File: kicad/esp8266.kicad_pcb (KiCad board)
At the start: 2 copper layers, 21 parts, among them J1 BATT, J2 Conn_Coaxial_Power, Q1 BSP75, U1 ESP-12E, U2 MCP73831-2-OT, U3 MCP1703A-3302_SOT23, U5 PCA9685PW, U6 Si7020-A20

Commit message: updates
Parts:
- added C6: 1uF, Capacitor_SMD:C_0805_2012Metric_Pad1.15x1.40mm_HandSolder, F.Cu at (280.5, 60.7)
- added C7: 1uF, Capacitor_SMD:C_0805_2012Metric_Pad1.15x1.40mm_HandSolder, F.Cu at (280.5, 62.6)
- added D3: D_Schottky, Diode_SMD:D_SOD-123, F.Cu at (249.1, 74.4)
- added D4: D_Schottky, Diode_SMD:D_SOD-123, F.Cu at (87.5, 72.5)
- added J3: CONN FT232RL, Connector_PinHeader_2.54mm:PinHeader_1x06_P2.54mm_Vertical, F.Cu at (87.5, 64.8)
- added J4: RJ12, Connector_RJ:RJ12_Amphenol_54601, F.Cu at (93.0, 127.0)
- added J5: RJ12, Connector_RJ:RJ12_Amphenol_54601, F.Cu at (93.0, 147.0)
- added J6: Onewire, Connector_Audio:Jack_3.5mm_Ledino_KB3SPRS_Horizontal, F.Cu at (168.0, 117.0)
- added J7: Onewire, Connector_Audio:Jack_3.5mm_Ledino_KB3SPRS_Horizontal, F.Cu at (193.0, 107.0)
- added Q2: BSP75, Package_TO_SOT_SMD:SOT-223-3_TabPin2, F.Cu at (118.6, 128.1)
- added Q3: BSP75, Package_TO_SOT_SMD:SOT-223-3_TabPin2, F.Cu at (127.4, 128.1)
- added Q4: BSP75, Package_TO_SOT_SMD:SOT-223-3_TabPin2, F.Cu at (118.6, 135.3)
- added R10: 10k, Resistor_SMD:R_0805_2012Metric_Pad1.15x1.40mm_HandSolder, F.Cu at (249.1, 76.5)
- added R7: 10k, Resistor_SMD:R_0805_2012Metric_Pad1.15x1.40mm_HandSolder, F.Cu at (215.2, 129.2)
- added R8: 10k, Resistor_SMD:R_0805_2012Metric_Pad1.15x1.40mm_HandSolder, F.Cu at (114.0, 72.5)
- added R9: 4.7k, Resistor_SMD:R_0805_2012Metric_Pad1.15x1.40mm_HandSolder, F.Cu at (245.3, 80.8)
- added SW1: RESET, digikey-footprints:Switch_Tactile_SMD_6x6mm, F.Cu at (149.1, 66.8)
- added SW2: PROG, digikey-footprints:Switch_Tactile_SMD_6x6mm, F.Cu at (149.1, 76.9)
- added TP1: TestPoint_2Pole, TestPoint:TestPoint_2Pads_Pitch2.54mm_Drill0.8mm, F.Cu at (258.4, 110.4)
- added U4: MS5637, libs:MS5637, F.Cu at (175.1, 58.4)
- R6: value 1M -> 270k
- U5: value PCA9685PW -> MCP1703A-5002_SOT23; footprint Package_SO:TSSOP-28_4.4x9.7mm_P0.65mm -> Package_TO_SOT_SMD:SOT-23
- moved J2 88.7 mm to (93.0, 112.0)
- moved U1 60.1 mm to (128.0, 67.0)
- moved R4 56.2 mm to (97.0, 76.2), turned to 180 degrees
- moved C1 53.9 mm to (101.3, 82.5)
- moved C2 53.9 mm to (93.8, 81.8)
- moved R1 53.9 mm to (97.5, 82.8)
- moved R3 52.4 mm to (101.6, 76.2), turned to 180 degrees
- moved R5 49.1 mm to (114.0, 64.8)
- moved C3 48.3 mm to (114.0, 69.9), turned to 180 degrees
- moved U2 46.9 mm to (107.2, 74.4), turned to 270 degrees
- moved R2 44.5 mm to (114.0, 75.0)
- moved R6 44.4 mm to (114.0, 67.4), turned to 180 degrees
- moved J1 44.1 mm to (108.5, 65.5), turned to 180 degrees
- moved D2 31.7 mm to (115.5, 81.4), turned to 180 degrees
- moved D1 31.4 mm to (115.5, 85.8)
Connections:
- net /MCP73831/STAT renamed /MCP73831/V_STATUS
- net Net-(C2-Pad1) renamed /VBAT
- net Net-(J2-Pad1) renamed +12V
- net Net-(U1-Pad16) renamed /IO15
- net Net-(U1-Pad19) renamed /SDA
- net Net-(U1-Pad20) renamed /SCL
- net Net-(U1-Pad5) renamed /IO14
- net Net-(U1-Pad6) renamed /IO12
- net Net-(U1-Pad7) renamed /IO13
- C3 pad 1: /MCP73831/VOLT -> /ADC
- C4 pad 2: VDD -> /MCP1703-33/VDD
- D1 pad 3: /MCP73831/VOUT -> /MCP1703-33/VDD
- D2 pad 1: /MCP73831/VOUT -> /MCP1703-33/VDD
- J2 pad 2: Net-(J2-Pad2) -> GND
- R5 pad 2: /MCP73831/VOLT -> /ADC
- R6 pad 1: /MCP73831/VOLT -> /ADC
- U1 pad 1: Net-(U1-Pad1) -> /RST
- U1 pad 15: Net-(U1-Pad15) -> GND
- U1 pad 17: Net-(U1-Pad17) -> /IO2
- U1 pad 2: Net-(U1-Pad2) -> /ADC
- U1 pad 21: Net-(U1-Pad21) -> /RX
- U1 pad 22: Net-(U1-Pad22) -> /TX
- U1 pad 3: Net-(U1-Pad3) -> /EN
- U1 pad 4: Net-(U1-Pad4) -> /RST
- U1 pad 8: Net-(U1-Pad8) -> +3V3
- U3 pad 3: VDD -> /MCP1703-33/VDD
- U5 pad 2: GND -> /MCP1703-50/3.3V
- U5 pad 3: GND -> /MCP1703-50/VDD
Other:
- board outline added: 100 x 100 mm

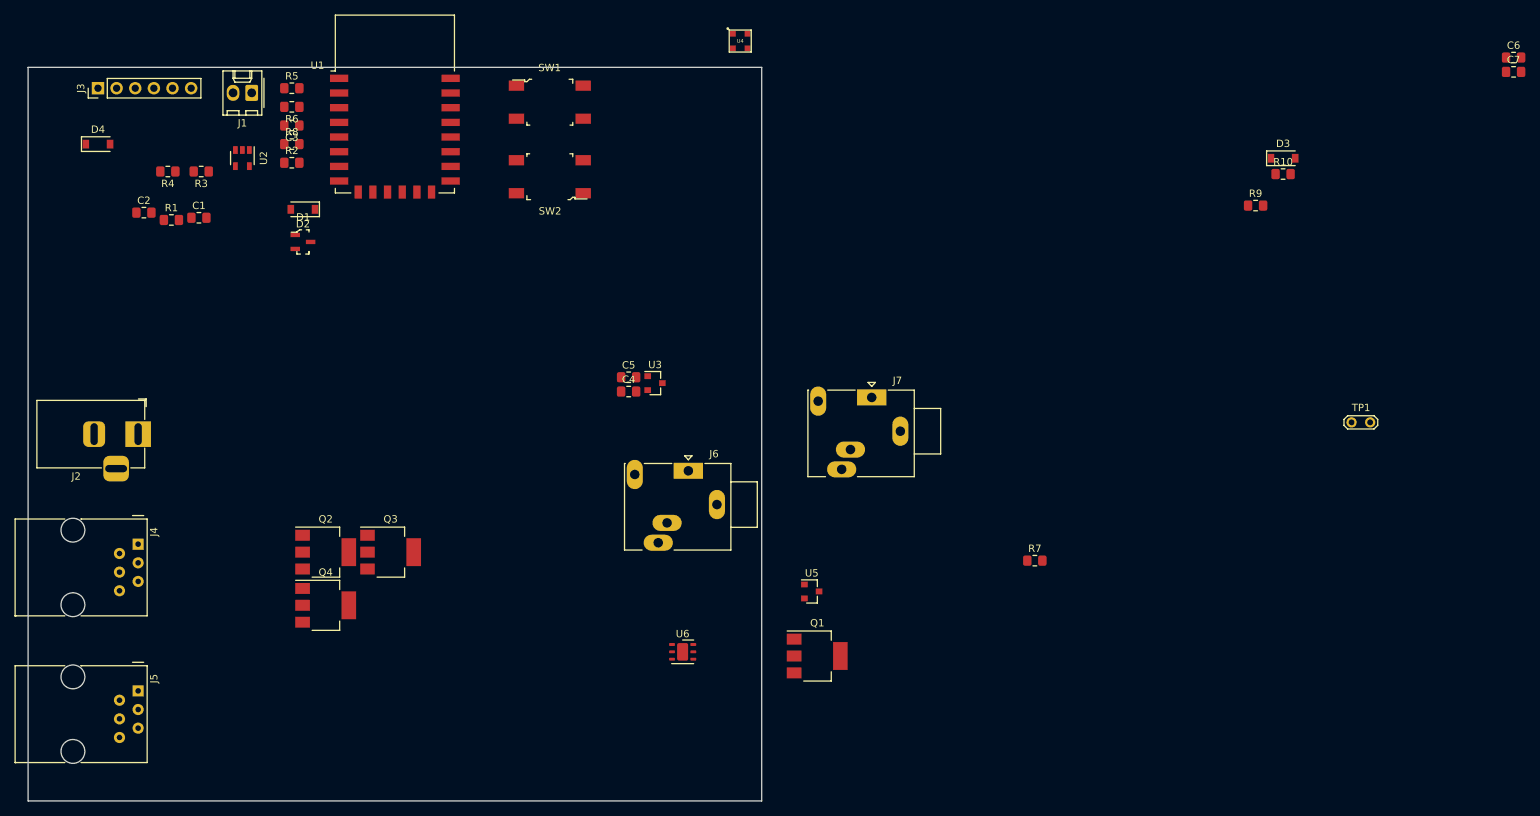
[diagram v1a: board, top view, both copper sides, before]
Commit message: add 18B20 on board
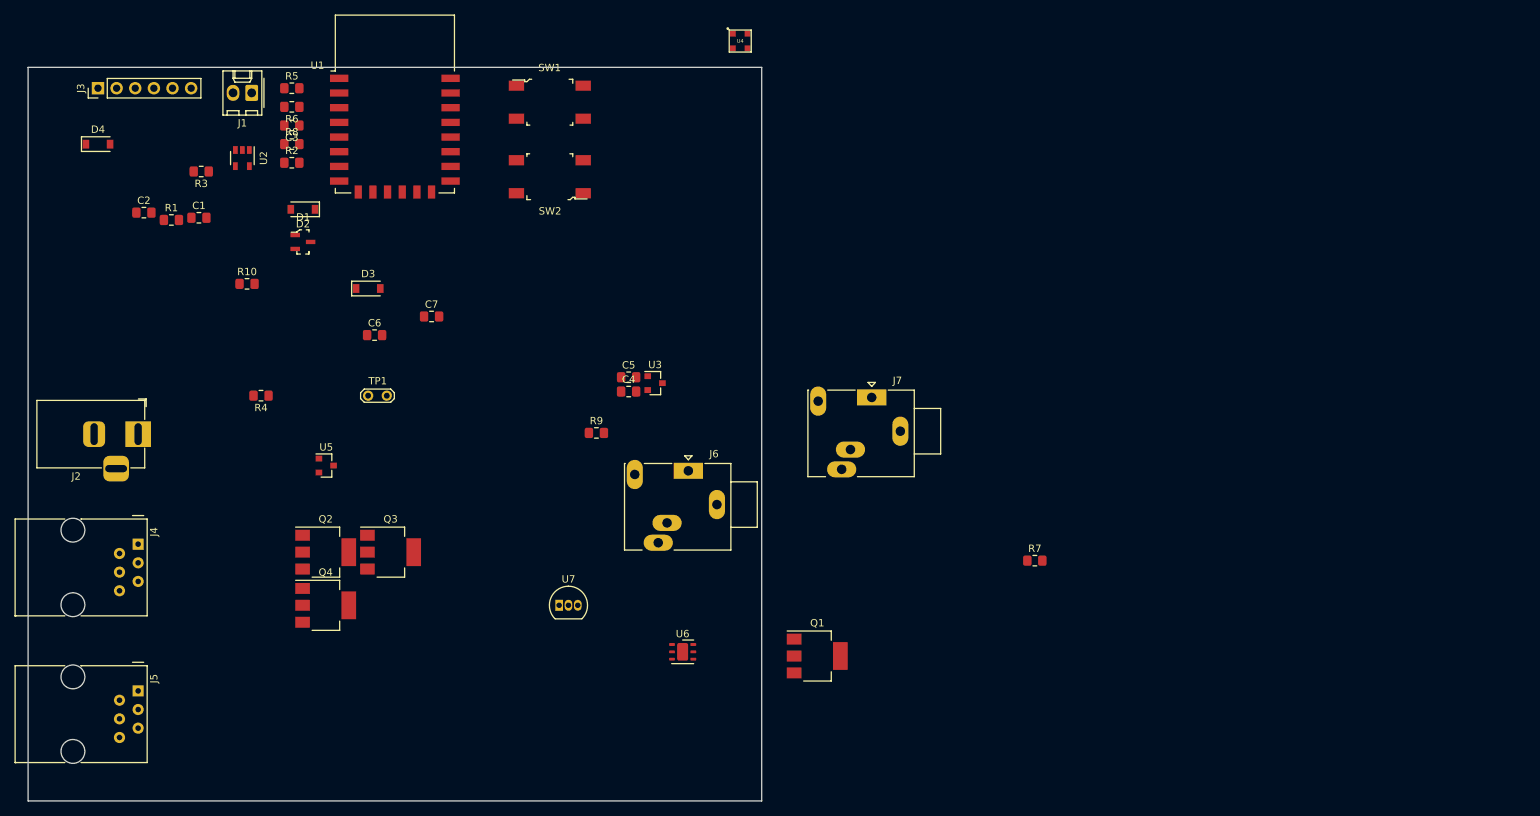
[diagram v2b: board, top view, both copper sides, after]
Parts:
- added U7: DS18B20, Package_TO_SOT_THT:TO-92_Inline, F.Cu at (150.4, 135.3)
- U2: value MCP73831-2-OT -> MCP73831-2
- moved C6 159.8 mm to (125.2, 98.5)
- moved C7 151.2 mm to (133.0, 96.0)
- moved R10 142.0 mm to (107.8, 91.5)
- moved TP1 134.1 mm to (124.4, 106.8)
- moved D3 126.0 mm to (124.4, 92.2)
- moved R9 95.0 mm to (155.5, 111.8)
- moved U5 68.4 mm to (118.6, 116.3)
- moved R4 33.1 mm to (109.8, 106.8)
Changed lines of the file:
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@@
     (tracks 0)
     (zones 0)
-    (modules 41)
-    (nets 74)
+    (modules 42)
+    (nets 77)
   )
   (page A4)
@@
   (net 72 /IO13)
   (net 73 /IO15)
+  (net 74 "Net-(U7-Pad2)")
+  (net 75 "Net-(U7-Pad3)")
+  (net 76 "Net-(U7-Pad1)")
   (net_class Default "This is the default net class."
     (clearance 0.2)
@@
     (add_net "Net-(U6-Pad6)")
     (add_net "Net-(U6-Pad7)")
+    (add_net "Net-(U7-Pad1)")
+    (add_net "Net-(U7-Pad2)")
+    (add_net "Net-(U7-Pad3)")
+  )
+  (module Package_TO_SOT_THT:TO-92_Inline (layer F.Cu)
+    (at 150.39 135.33)
+    (descr "TO-92 leads in-line, narrow, oval pads, drill 0.75mm (see NXP sot054_po.pdf)")
+    (tags "to-92 sc-43 sc-43a sot54 PA33 transistor")
+    (fp_text reference U7 (at 1.27 -3.56) (layer F.SilkS)
+      (effects (font (size 1 1) (thickness 0.15)))
+    )
+    (fp_text value DS18B20 (at 1.27 2.79) (layer F.Fab)
+      (effects (font (size 1 1) (thickness 0.15)))
+    )
+    (fp_text user %R (at 1.27 -3.56) (layer F.Fab)
+      (effects (font (size 1 1) (thickness 0.15)))
+    )
+    (fp_line (start -0.53 1.85) (end 3.07 1.85) (layer F.SilkS) (width 0.12))
+    (fp_line (start -0.5 1.75) (end 3 1.75) (layer F.Fab) (width 0.1))
+    (fp_line (start -1.46 -2.73) (end 4 -2.73) (layer F.CrtYd) (width 0.05))
+    (fp_line (start -1.46 -2.73) (end -1.46 2.01) (layer F.CrtYd) (width 0.05))
+    (fp_line (start 4 2.01) (end 4 -2.73) (layer F.CrtYd) (width 0.05))
+    (fp_line (start 4 2.01) (end -1.46 2.01) (layer F.CrtYd) (width 0.05))
+    (fp_arc (start 1.27 0) (end 1.27 -2.48) (angle 135) (layer F.Fab) (width 0.1))
+    (fp_arc (start 1.27 0) (end 1.27 -2.6) (angle -135) (layer F.SilkS) (width 0.12))
+    (fp_arc (start 1.27 0) (end 1.27 -2.48) (angle -135) (layer F.Fab) (width 0.1))
+    (fp_arc (start 1.27 0) (end 1.27 -2.6) (angle 135) (layer F.SilkS) (width 0.12))
+    (pad 2 thru_hole oval (at 1.27 0) (size 1.05 1.5) (drill 0.75) (layers *.Cu *.Mask)
+      (net 74 "Net-(U7-Pad2)"))
+    (pad 3 thru_hole oval (at 2.54 0) (size 1.05 1.5) (drill 0.75) (layers *.Cu *.Mask)
+      (net 75 "Net-(U7-Pad3)"))
+    (pad 1 thru_hole rect (at 0 0) (size 1.05 1.5) (drill 0.75) (layers *.Cu *.Mask)
+      (net 76 "Net-(U7-Pad1)"))
+    (model ${KISYS3DMOD}/Package_TO_SOT_THT.3dshapes/TO-92_Inline.wrl
+      (at (xyz 0 0 0))
+      (scale (xyz 1 1 1))
+      (rotate (xyz 0 0 0))
+    )
   )
   (module Capacitor_SMD:C_0805_2012Metric_Pad1.15x1.40mm_HandSolder (layer F.Cu)
@@
   )
   (module Resistor_SMD:R_0805_2012Metric_Pad1.15x1.40mm_HandSolder (layer F.Cu)
-    (at 97.05 76.2 180)
+    (at 109.75 106.755 180)
     (descr "Resistor SMD 0805 (2012 Metric), square (rectangular) end terminal, IPC_7351 nominal with elongated pad for handsoldering. (Body size source: https://docs.google.com/spreadsheets/d/1BsfQQcO9C6DZCsRaXUlFlo91Tg2WpOkGARC1WS5S8t0/edit?usp=sharing), generated with kicad-footprint-generator")
     (tags "resistor handsolder")
@@
       (effects (font (size 1 1) (thickness 0.15)))
     )
-    (fp_text value MCP73831-2-OT (at 0 2.9 270) (layer F.Fab)
+    (fp_text value MCP73831-2 (at 0 2.9 270) (layer F.Fab)
       (effects (font (size 1 1) (thickness 0.15)))
     )
@@
   )
   (module TestPoint:TestPoint_2Pads_Pitch2.54mm_Drill0.8mm (layer F.Cu)
-    (at 258.405001 110.395001)
+    (at 124.355 106.755)
     (descr "Test point with 2 pins, pitch 2.54mm, drill diameter 0.8mm")
     (tags "CONN DEV")
@@
   )
   (module Capacitor_SMD:C_0805_2012Metric_Pad1.15x1.40mm_HandSolder (layer F.Cu)
-    (at 280.495001 60.665001)
+    (at 125.235 98.5)
     (descr "Capacitor SMD 0805 (2012 Metric), square (rectangular) end terminal, IPC_7351 nominal with elongated pad for handsoldering. (Body size source: https://docs.google.com/spreadsheets/d/1BsfQQcO9C6DZCsRaXUlFlo91Tg2WpOkGARC1WS5S8t0/edit?usp=sharing), generated with kicad-footprint-generator")
     (tags "capacitor handsolder")
@@
   )
   (module Capacitor_SMD:C_0805_2012Metric_Pad1.15x1.40mm_HandSolder (layer F.Cu)
-    (at 280.495001 62.615001)
+    (at 133 95.96)
     (descr "Capacitor SMD 0805 (2012 Metric), square (rectangular) end terminal, IPC_7351 nominal with elongated pad for handsoldering. (Body size source: https://docs.google.com/spreadsheets/d/1BsfQQcO9C6DZCsRaXUlFlo91Tg2WpOkGARC1WS5S8t0/edit?usp=sharing), generated with kicad-footprint-generator")
     (tags "capacitor handsolder")
@@
   )
   (module Diode_SMD:D_SOD-123 (layer F.Cu)
-    (at 249.075001 74.395001)
+    (at 124.355 92.15)
     (descr SOD-123)
     (tags SOD-123)
@@
   )
   (module Resistor_SMD:R_0805_2012Metric_Pad1.15x1.40mm_HandSolder (layer F.Cu)
-    (at 245.325001 80.845001)
+    (at 155.47 111.835)
     (descr "Resistor SMD 0805 (2012 Metric), square (rectangular) end terminal, IPC_7351 nominal with elongated pad for handsoldering. (Body size source: https://docs.google.com/spreadsheets/d/1BsfQQcO9C6DZCsRaXUlFlo91Tg2WpOkGARC1WS5S8t0/edit?usp=sharing), generated with kicad-footprint-generator")
     (tags "resistor handsolder")
@@
   )
   (module Resistor_SMD:R_0805_2012Metric_Pad1.15x1.40mm_HandSolder (layer F.Cu)
-    (at 249.075001 76.545001)
+    (at 107.845 91.515)
     (descr "Resistor SMD 0805 (2012 Metric), square (rectangular) end terminal, IPC_7351 nominal with elongated pad for handsoldering. (Body size source: https://docs.google.com/spreadsheets/d/1BsfQQcO9C6DZCsRaXUlFlo91Tg2WpOkGARC1WS5S8t0/edit?usp=sharing), generated with kicad-footprint-generator")
     (tags "resistor handsolder")
@@
   )
   (module Package_TO_SOT_SMD:SOT-23 (layer F.Cu)
-    (at 184.825001 133.445001)
+    (at 118.64 116.28)
     (descr "SOT-23, Standard")
     (tags SOT-23)

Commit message: correst bsp75 footprint
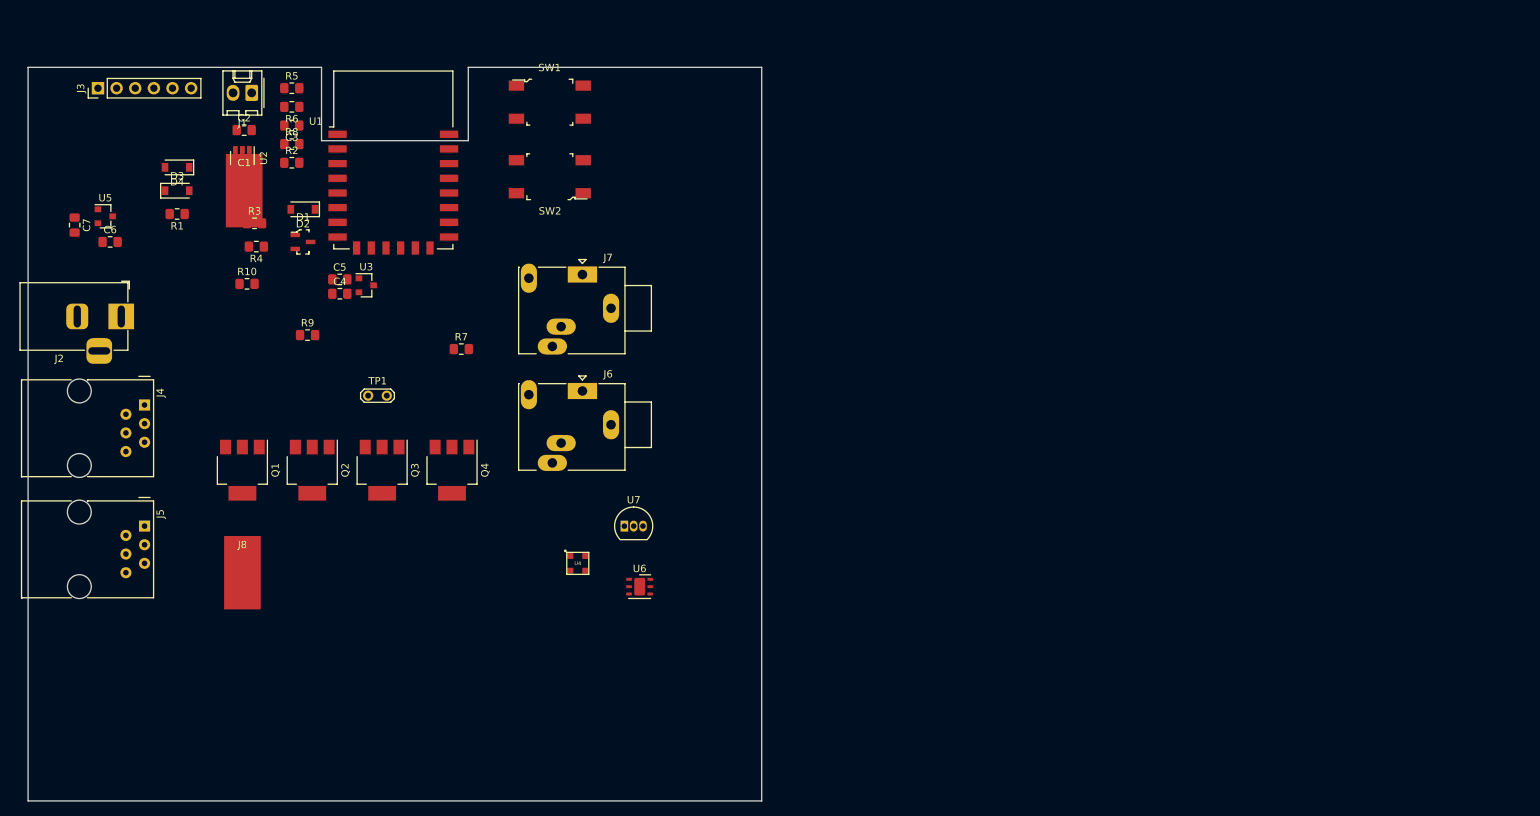
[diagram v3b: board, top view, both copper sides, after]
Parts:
- added J8: Conn_01x01_Male, Connector_Wire:SolderWirePad_1x01_SMD_5x10mm, F.Cu at (107.2, 130.9)
- C1: footprint Capacitor_SMD:C_0805_2012Metric_Pad1.15x1.40mm_HandSolder -> Connector_Wire:SolderWirePad_1x01_SMD_5x10mm
- Q1, Q2, Q3, Q4: footprint Package_TO_SOT_SMD:SOT-223-3_TabPin2 -> Package_TO_SOT_SMD:SOT-223
- moved R7 83.3 mm to (137.1, 100.4)
- moved Q1 82.4 mm to (107.2, 116.9), turned to 270 degrees
- moved U4 74.6 mm to (152.9, 129.6)
- moved C7 50.2 mm to (84.3, 83.5), turned to 270 degrees
- moved U5 45.4 mm to (88.5, 82.3)
- moved J7 42.8 mm to (153.6, 90.2)
- moved C4 41.6 mm to (120.5, 92.9)
- moved C5 41.6 mm to (120.5, 90.9)
- moved R9 41.6 mm to (116.1, 98.5)
- moved U3 41.6 mm to (124.1, 91.7)
- moved C6 38.2 mm to (89.2, 85.8)
- moved D3 29.3 mm to (98.3, 78.8)
- moved Q4 25.2 mm to (135.8, 116.9), turned to 270 degrees
- moved J5 22.5 mm to (93.9, 124.5)
- moved R4 20.3 mm to (109.1, 86.4)
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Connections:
- Q1 pad 1: Net-(Q1-Pad1) -> /IO12
- Q1 pad 3: Net-(Q1-Pad3) -> GND
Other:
- outline, holes or cut-outs redrawn
